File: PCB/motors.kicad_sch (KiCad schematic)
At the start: 11 parts, among them U4 MAX22201ATC+

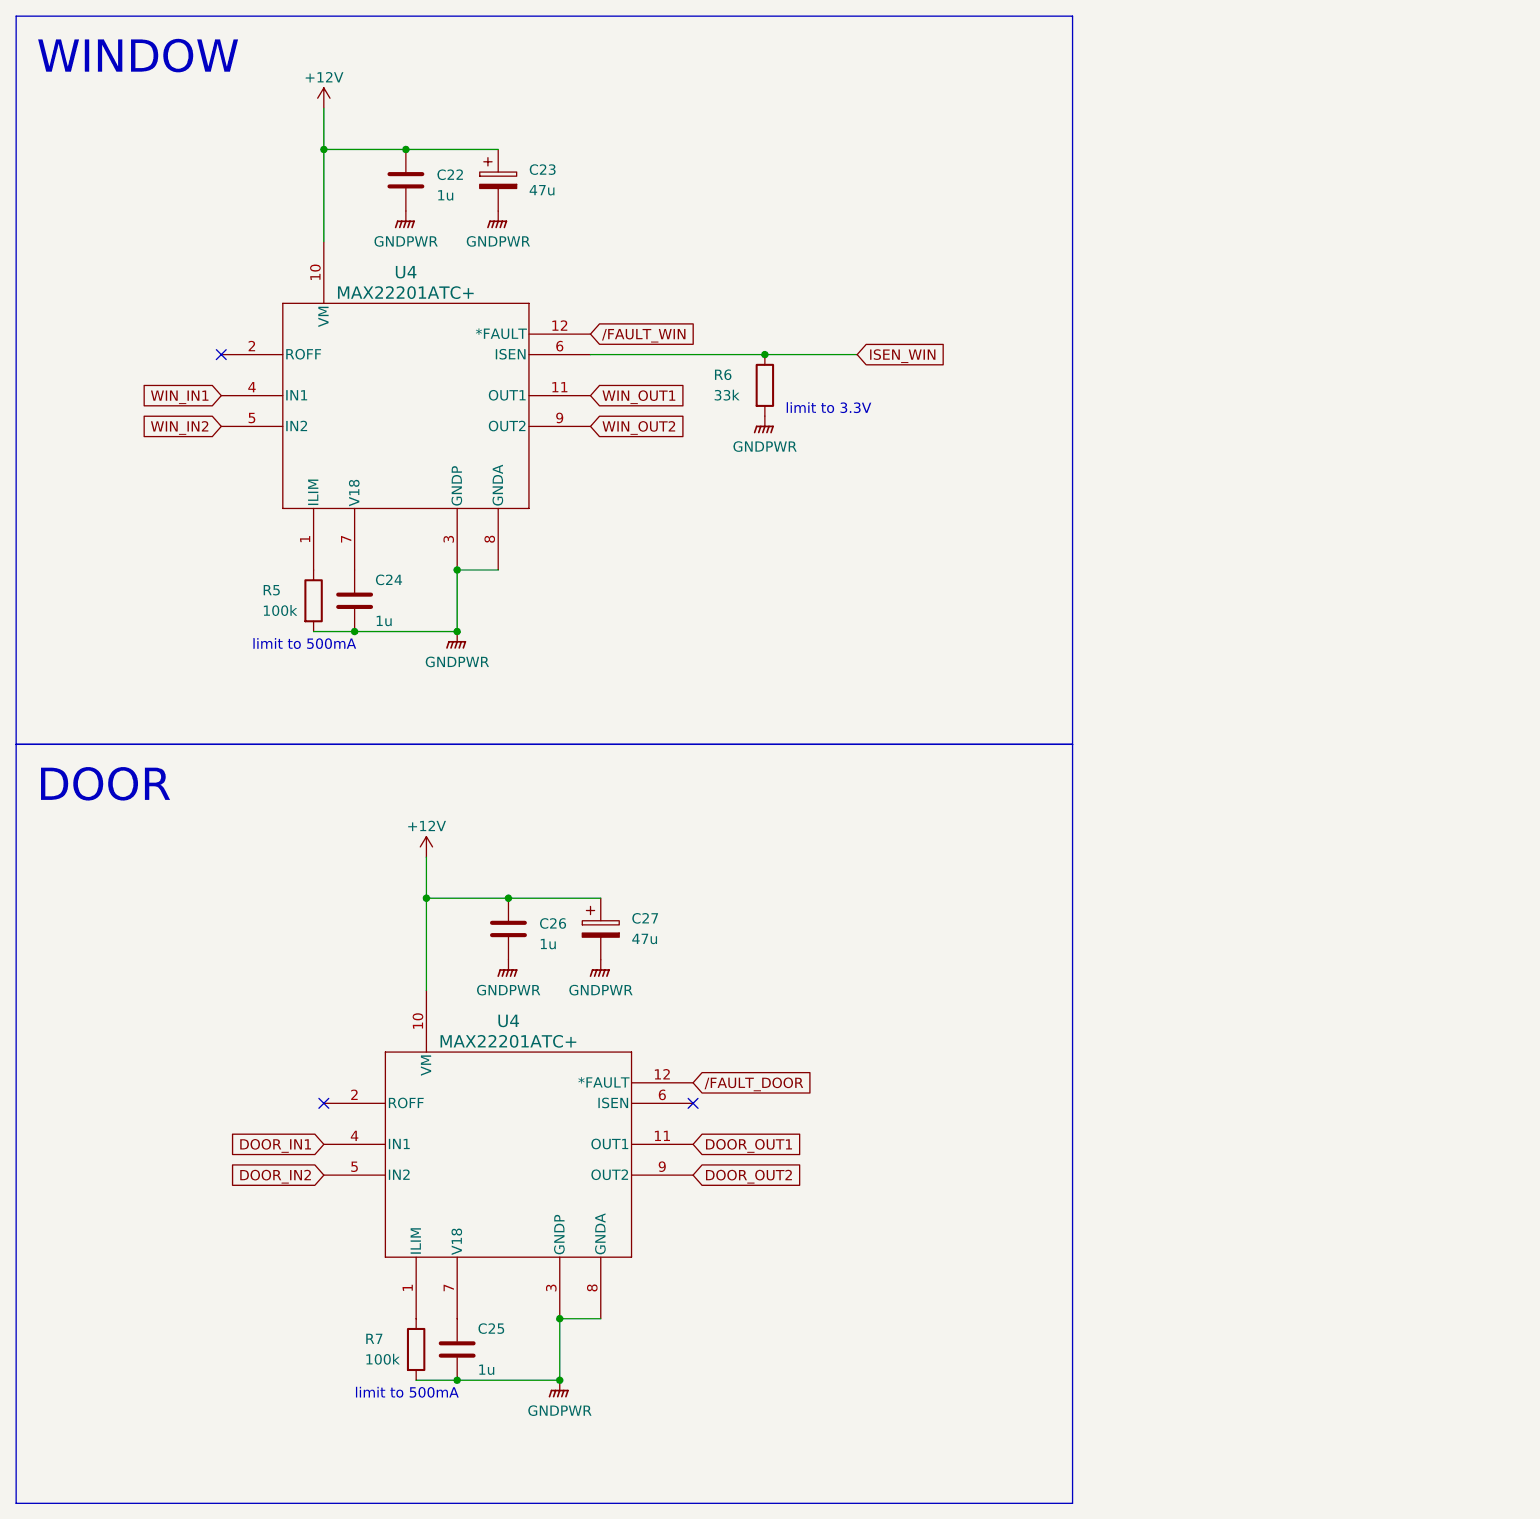
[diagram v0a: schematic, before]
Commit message: change file structure
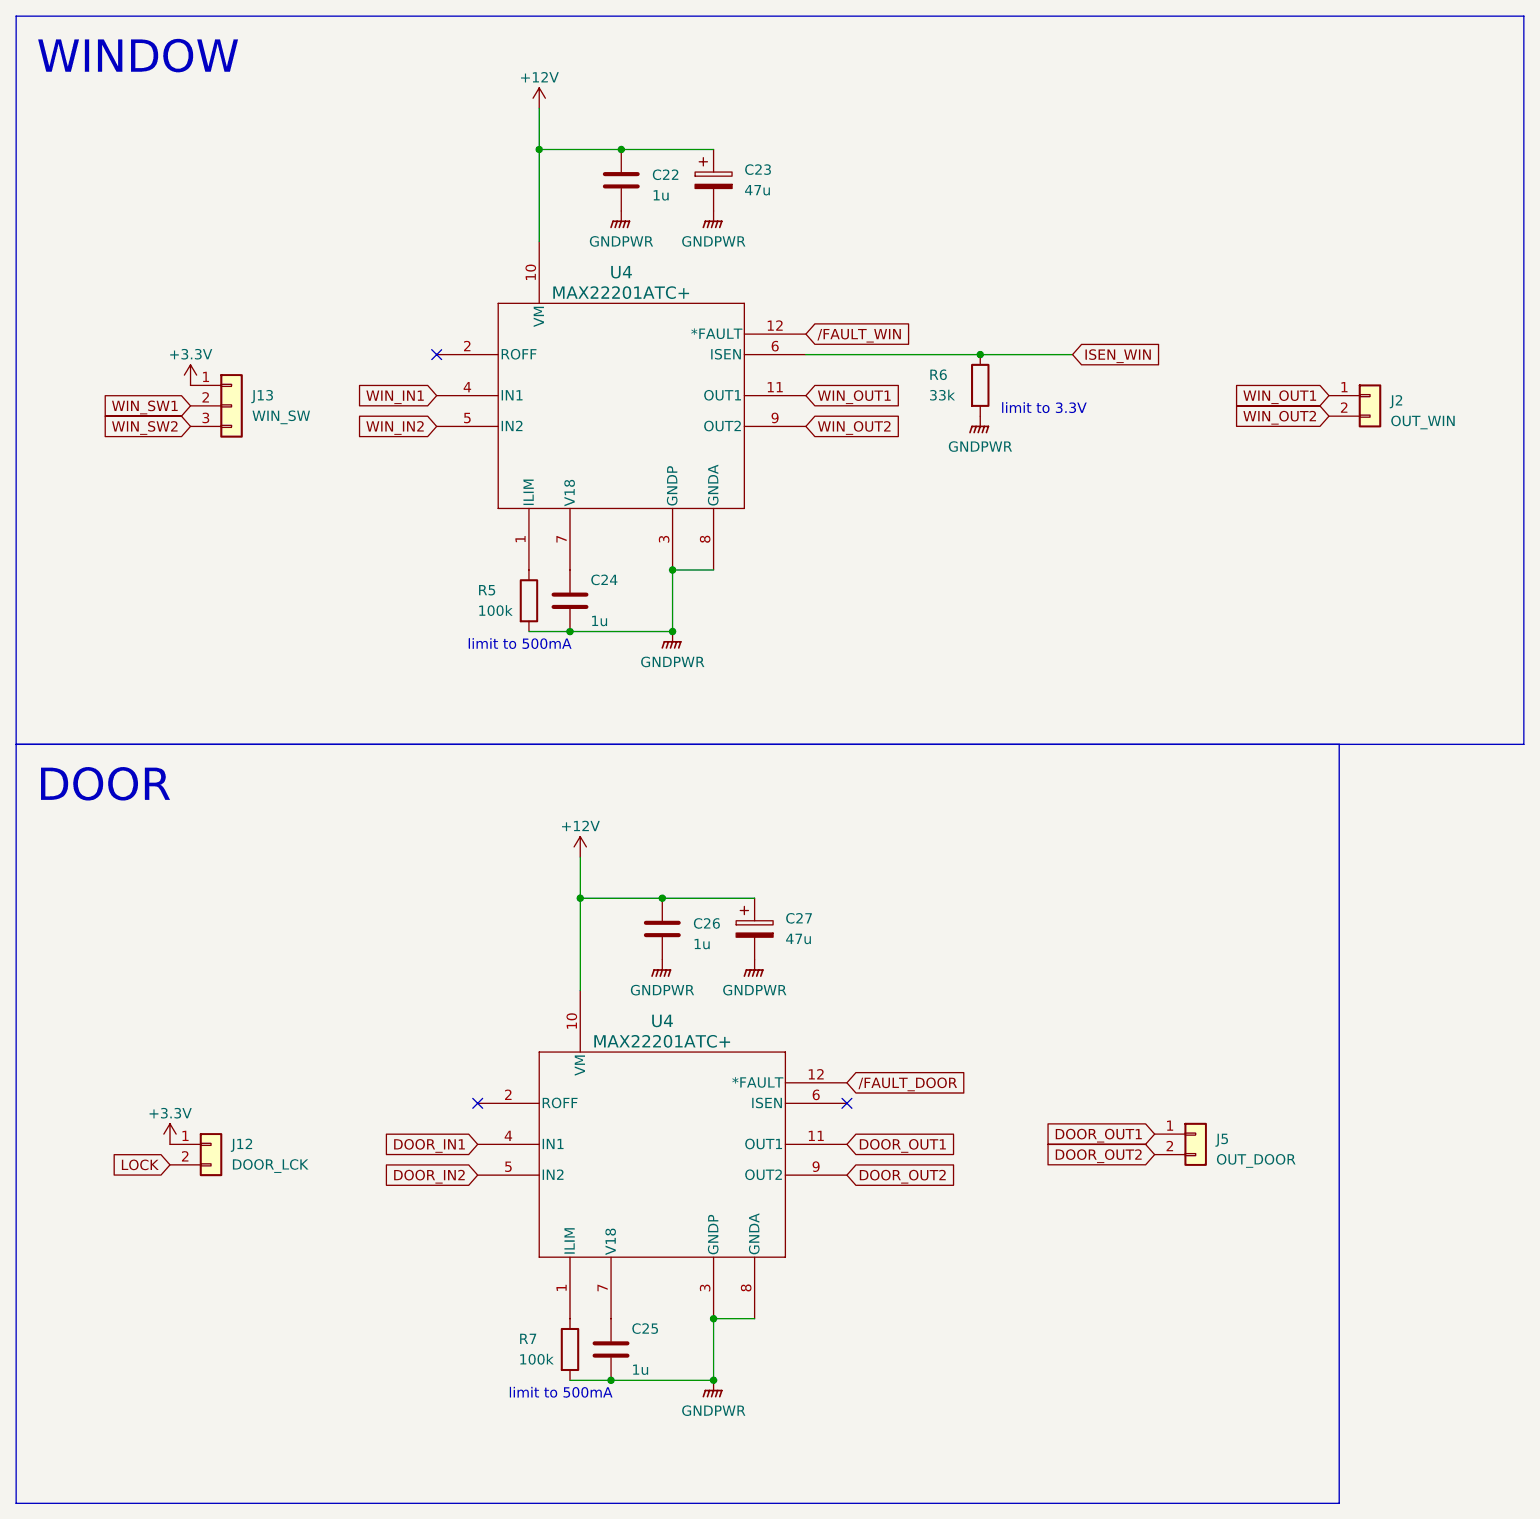
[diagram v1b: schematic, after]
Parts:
- added J12: DOOR_LCK, symbol Connector_Generic:Conn_01x02
- added J13: WIN_SW, symbol Connector_Generic:Conn_01x03
- added J2: OUT_WIN, symbol Connector_Generic:Conn_01x02
- added J5: OUT_DOOR, symbol Connector_Generic:Conn_01x02
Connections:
- net DOOR_OUT1: now also J5.1 (Pin_1)
- net DOOR_OUT2: now also J5.2 (Pin_2)
- net WIN_OUT1: now also J2.1 (Pin_1)
- net WIN_OUT2: now also J2.2 (Pin_2)
- new net +3.3V: J12.1 (Pin_1), J13.1 (Pin_1)
- new net LOCK: J12.2 (Pin_2)
- new net WIN_SW1: J13.2 (Pin_2)
- new net WIN_SW2: J13.3 (Pin_3)
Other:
- moved on the sheet: C22, C23, C24, C25, C26, C27, R5, R6, R7, U4

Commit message: changed to DCDC 3.3V, added extra bit for window ctrl + misc corrections
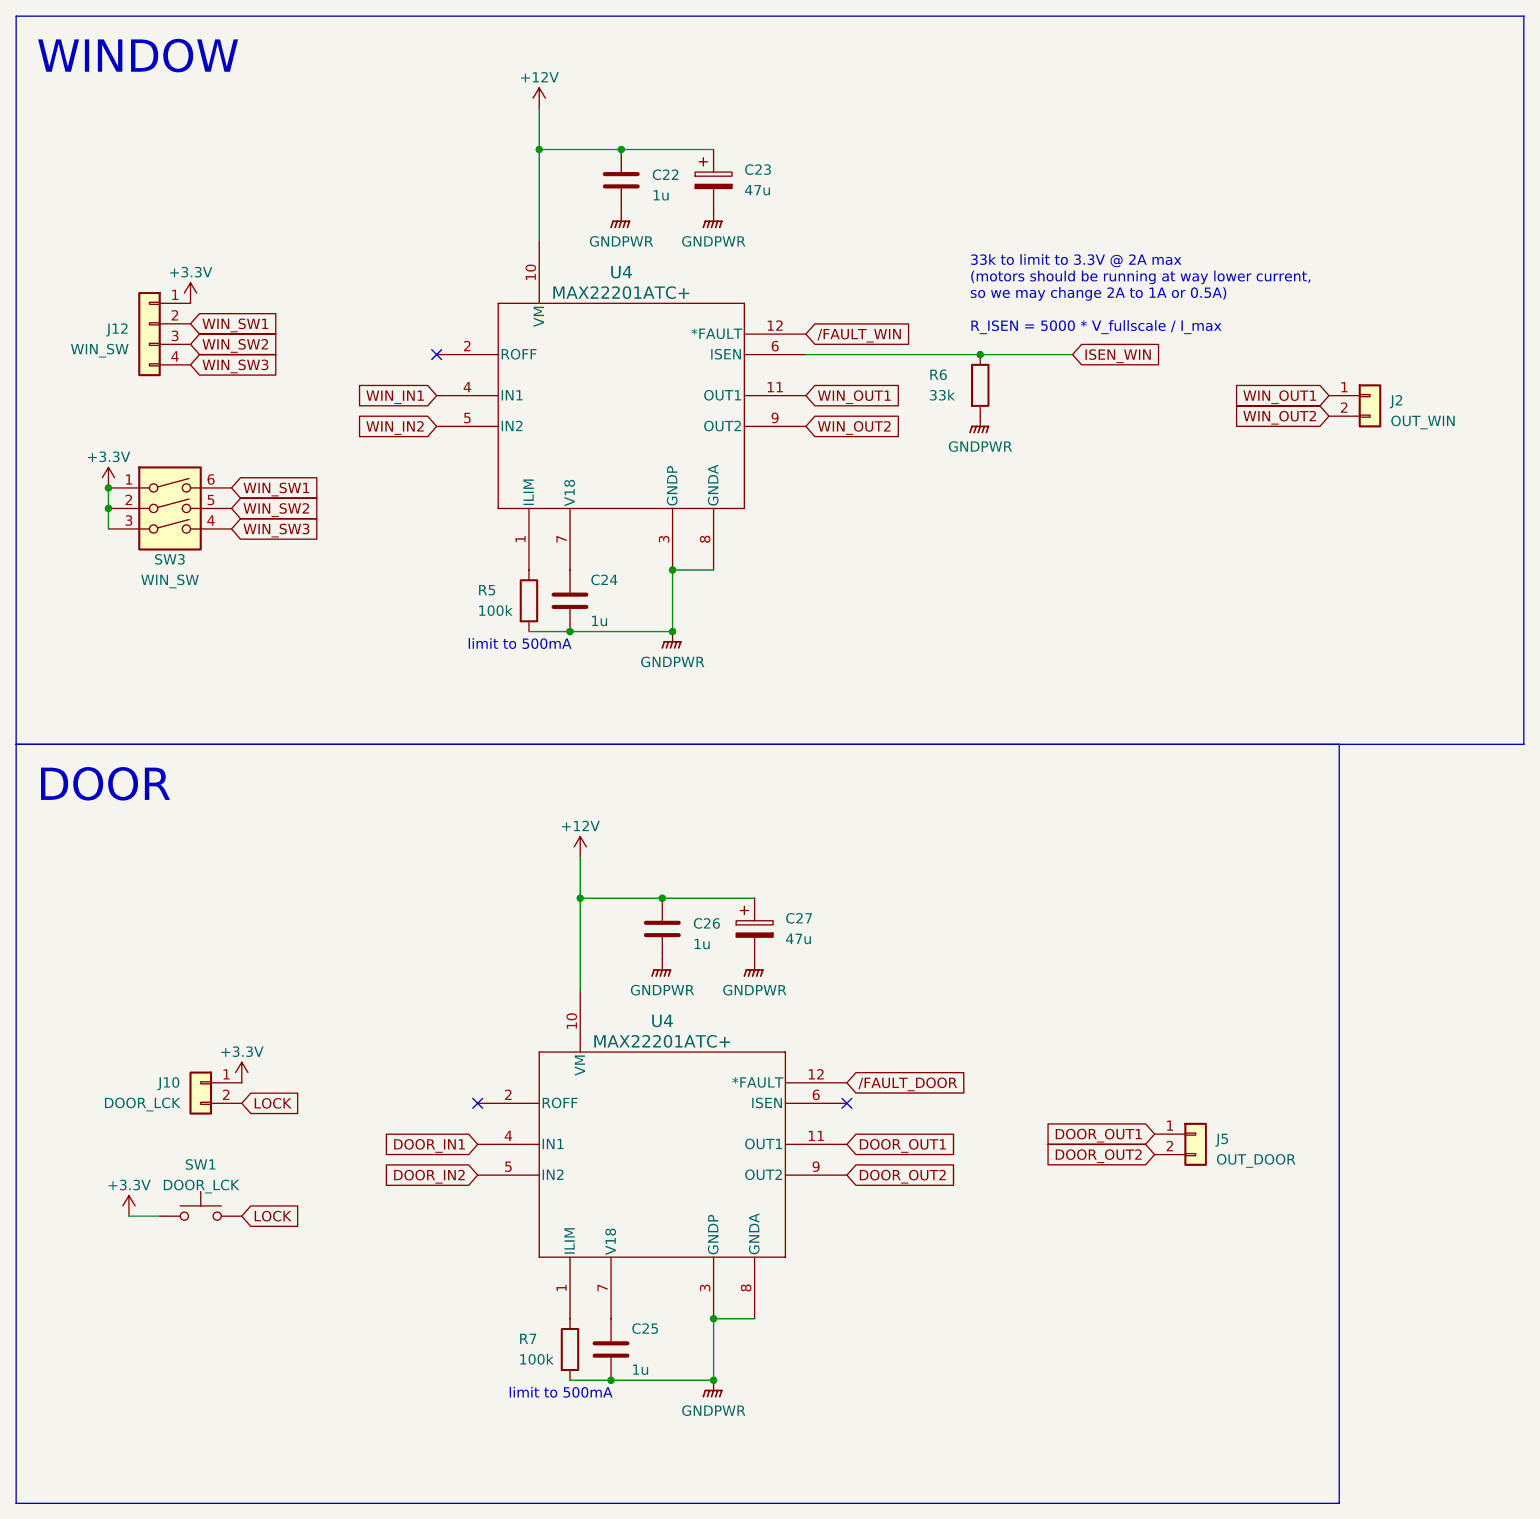
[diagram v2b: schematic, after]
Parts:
- removed J13: WIN_SW, symbol Connector_Generic:Conn_01x03
- added J12: WIN_SW, symbol Connector_Generic:Conn_01x04
- added SW1: DOOR_LCK, symbol Switch:SW_Push
- added SW3: WIN_SW, symbol Switch:SW_DIP_x03
- renumbered J12 to J10
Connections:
- net +3.3V: now also J12.1 (Pin_1), SW1.1, SW3.1, SW3.2, SW3.3
- net LOCK: now also SW1.2
- net WIN_SW1: now also J12.2 (Pin_2), SW3.6
- net WIN_SW2: now also J12.3 (Pin_3), SW3.5
- new net WIN_SW3: J12.4 (Pin_4), SW3.4
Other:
- note added: "33k to limit to 3.3V @ 2A max (motors should be running at way lower current, so we may change 2A to 1A or 0.5A) R_ISEN = 5000 * V_fullscale / I_max"
- note removed: "limit to 3.3V"
- moved on the sheet: J10
